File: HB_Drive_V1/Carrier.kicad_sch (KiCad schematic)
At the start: 33 parts, among them U10 NE555D, U11 TL082, U22 NE555D

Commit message: finishes hirearchical labels, add 10v +- ref generation and updates the DC offset circuits
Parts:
- removed R35, R42: PV36W104C01B00, PV36W104C01B00:POT_PV36W_BRN, symbol PV36W104C01B00:PV36W104C01B00
- removed R38, R39, R41: 51KΩ, Resistor_SMD:R_0603_1608Metric_Pad0.98x0.95mm_HandSolder, symbol Device:R_Small_US
- removed R40: 10KΩ, Resistor_SMD:R_0603_1608Metric_Pad0.98x0.95mm_HandSolder, symbol Device:R_Small_US
- removed TP8: TestPoint, TestPoint:TestPoint_Loop_D2.60mm_Drill1.6mm_Beaded, symbol Connector:TestPoint
- removed unit 2 of U11
- added C50, C51: 100pF 50V, Capacitor_SMD:C_0603_1608Metric, symbol Device:C
- added R100: PV36W104C01B00, PV36W104C01B00:POT_PV36W_BRN, symbol PV36W104C01B00:PV36W104C01B00
- added R101, R102: 10KΩ, Resistor_SMD:R_0603_1608Metric_Pad0.98x0.95mm_HandSolder, symbol Device:R_Small_US
- added R103: PV36W204C01B00, PV36W104C01B00:POT_PV36W_BRN, symbol PV36W104C01B00:PV36W104C01B00
- added TP28: TestPoint, TestPoint:TestPoint_Loop_D2.60mm_Drill1.6mm_Beaded, symbol Connector:TestPoint
- added U26: TL082, Package_SO:SOIC-8_5.3x5.3mm_P1.27mm, symbol Amplifier_Operational:TL082
- added U27: TL082, symbol Amplifier_Operational:TL082
- renumbered C18 to C41, C19 to C42, C20 to C43, C21 to C44, C22 to C45, C23 to C46, C24 to C47, C39 to C48, C42 to C49, D7 to D5, R36 to R74, R37 to R75, R43 to R81, R44 to R82, R45 to R83, R46 to R84, R71 to R85, R70 to R86, R57 to R87, TP7 to TP20, TP9 to TP22, TP10 to TP23, U10 to U19, U11 to U20, U22 to U21
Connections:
- net Bipolar Triangle Wave: now also R101.2
- net Carrier: now also R103.2, R103.3, TP28.1, U27.7
- net GND: now also U27.6 (-)
- new net: R101.1, R102.1, R103.1, U27.5 (+)
- new net: R100.2, U26.5 (+)
- new net: R102.2, U26.6 (-), U26.7
- new net +10V_Ref: R100.1
- new net -10V_Ref: R100.3
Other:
- note added: "DC Offset [0 to -10V DC]"
- note added: "TRIANGLE WAVE DC OFFSET, AND GAIN ADJUST"
- note removed: "DC Offset [0 to -15V DC]"
- note removed: "TRIANGLE WAVE DC OFFSET AND GAIN ADJUST"

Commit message: updates board to highest working copy
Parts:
- removed C46, C47: 100nF 100V, Capacitor_SMD:C_0603_1608Metric, symbol Device:C
- removed unit 3 of U20
- removed U27: TL082, symbol Amplifier_Operational:TL082
- added C1001: 100pF 50V, Capacitor_SMD:C_0603_1608Metric, symbol Device:C
- added C1009, C1011, C1013, C1014: 100nF 100V, Capacitor_SMD:C_0603_1608Metric, symbol Device:C
- added J1001: Conn_02x02_Odd_Even, Connector_PinHeader_2.54mm:PinHeader_2x02_P2.54mm_Vertical, symbol Connector_Generic:Conn_02x02_Odd_Even
- added unit 3 of U1003
- added U1004: TL082, Package_SO:SOIC-8_3.9x4.9mm_P1.27mm, symbol Amplifier_Operational:TL082
- C1002: renamed from C51; now not fitted
- C1003: renamed from C50; now not fitted
- U1002: renamed from U21; now not fitted
- U1003: renamed from U20; footprint Package_SO:SOIC-8_5.3x5.3mm_P1.27mm -> Package_SO:SOIC-8_3.9x4.9mm_P1.27mm
- U1003: renamed from U26; footprint Package_SO:SOIC-8_5.3x5.3mm_P1.27mm -> Package_SO:SOIC-8_3.9x4.9mm_P1.27mm
- renumbered C41 to C1004, C42 to C1005, C43 to C1006, C44 to C1007, C45 to C1008, C48 to C1010, C49 to C1012, D5 to D1001, D6 to D1002, R74 to R1001, R75 to R1002, R100 to R1003, R101 to R1004, R102 to R1005, R81 to R1006, R103 to R1007, R82 to R1008, R83 to R1009, R84 to R1010, R85 to R1011, R86 to R1012, R87 to R1013, TP20 to TP1001, TP22 to TP1002, TP28 to TP1003, TP23 to TP1004, U19 to U1001
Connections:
- net +15V: now also C1013.2, C1014.2, U1003.8 (V+), U1004.8 (V+)
- net -15V: now also C1009.1, C1011.1, U1003.4 (V-), U1004.4 (V-)
- net Carrier: now also U1004.7
- net GND: now also C1002.2, C1003.2, C1001.2, C1009.2, C1011.2, C1013.1, C1014.1, U1004.5 (+)
- net at C1004.1, R1002.2, U1001.2 (TRIG)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: now also C1002.1, C1003.1, C1001.1
- net at R1004.1, R1005.1, R1007.1: now also U1004.6 (-)
- net at C1010.1, D1001.2 (A), D1002.1 (K)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: no longer R1012.1
- net at D1001.1 (K): now also R1012.1
- net at TP1001.1, U1001.3 (OUT): now also J1001.3 (Pin_3); no longer C1006.2
- net Experimental Square Wave: now reaches U1002.3 (OUT)
- net Experimental Square Wave: now also J1001.1 (Pin_1)
- new net: C1006.2, J1001.2 (Pin_2), J1001.4 (Pin_4)
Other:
- moved on the sheet: D1001, D1002, R1003, R1007, R1008, R1012, TP1001, TP1002, TP1003, TP1004, U1001, U1003A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

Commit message: updates board to REV 1 Ordered version
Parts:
- added unit 1 of U1004
- R1004, R1005, R1009: value 10KΩ -> 10kΩ 1%
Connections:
- net GND: now also U1004.3 (+)
- new net: U1004.1, U1004.2 (-)
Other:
- note added: "unused OpAmp 1004A on TL082 Dual Package"
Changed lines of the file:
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@@
 	)
 	(rectangle
+		(start 87.63 95.25)
+		(end 138.43 99.06)
+		(stroke
+			(width 0)
+			(type default)
+		)
+		(fill
+			(type none)
+		)
+	)
+	(rectangle
 		(start 29.718 37.338)
 		(end 53.848 43.688)
@@
 		)
 	)
+	(text "unused OpAmp 1004A on TL082 Dual Package"
+		(exclude_from_sim no)
+		(at 113.03 97.282 0)
+		(effects
+			(font
+				(size 1.27 1.27)
+			)
+		)
+	)
 	(text "TRIANGLE WAVE DC OFFSET, AND GAIN ADJUST"
 		(exclude_from_sim no)
@@
 	(wire
 		(pts
+			(xy 76.2 110.49) (xy 91.44 110.49)
+		)
+		(stroke
+			(width 0)
+			(type default)
+		)
+	)
+	(wire
+		(pts
 			(xy 194.31 105.41) (xy 194.31 106.68)
 		)
@@
 	(wire
 		(pts
+			(xy 72.39 99.06) (xy 72.39 101.6)
+		)
+		(stroke
+			(width 0)
+			(type default)
+		)
+	)
+	(wire
+		(pts
 			(xy 105.41 110.49) (xy 105.41 118.11)
 		)
@@
 	(wire
 		(pts
+			(xy 91.44 101.6) (xy 91.44 110.49)
+		)
+		(stroke
+			(width 0)
+			(type default)
+		)
+	)
+	(wire
+		(pts
 			(xy 64.77 45.72) (xy 64.77 46.99)
 		)
@@
 	(wire
 		(pts
+			(xy 72.39 99.06) (xy 76.2 99.06)
+		)
+		(stroke
+			(width 0)
+			(type default)
+		)
+	)
+	(wire
+		(pts
 			(xy 179.07 106.68) (xy 181.61 106.68)
 		)
@@
 	(wire
 		(pts
+			(xy 76.2 104.14) (xy 76.2 110.49)
+		)
+		(stroke
+			(width 0)
+			(type default)
+		)
+	)
+	(wire
+		(pts
 			(xy 45.72 110.49) (xy 52.07 110.49)
 		)
@@
 	)
 	(symbol
+		(lib_id "Amplifier_Operational:TL082")
+		(at 83.82 101.6 0)
+		(unit 1)
+		(body_style 1)
+		(exclude_from_sim no)
+		(in_bom yes)
+		(on_board yes)
+		(in_pos_files yes)
+		(dnp no)
+		(property "Reference" "U1004"
+			(at 86.614 106.426 0)
+			(show_name no)
+			(do_not_autoplace no)
+			(effects
+				(font
+					(size 1.27 1.27)
+				)
+			)
+		)
+		(property "Value" "TL082"
+			(at 87.884 107.188 0)
+			(hide yes)
+			(show_name no)
+			(do_not_autoplace no)
+			(effects
+				(font
+					(size 1.27 1.27)
+				)
+			)
+		)
+		(property "Footprint" "Package_SO:SOIC-8_3.9x4.9mm_P1.27mm"
+			(at 83.82 101.6 0)
+			(hide yes)
+			(show_name no)
+			(do_not_autoplace no)
+			(effects
+				(font
+					(size 1.27 1.27)
+				)
+			)
+		)
+		(property "Datasheet" "http://www.ti.com/lit/ds/symlink/tl081.pdf"
+			(at 83.82 101.6 0)
+			(hide yes)
+			(show_name no)
+			(do_not_autoplace no)
+			(effects
+				(font
+					(size 1.27 1.27)
+				)
+			)
+		)
+		(property "Description" "Dual JFET-Input Operational Amplifiers, DIP-8/SOIC-8/SSOP-8"
+			(at 83.82 101.6 0)
+			(hide yes)
+			(show_name no)
+			(do_not_autoplace no)
+			(effects
+				(font
+					(size 1.27 1.27)
+				)
+			)
+		)
+		(pin "3"
+		)
+		(pin "1"
+		)
+		(pin "2"
+		)
+		(pin "6"
+		)
+		(pin "4"
+		)
+		(pin "7"
+		)
+		(pin "5"
+		)
+		(pin "8"
+		)
+		(instances
+			(project "HB_Drive_V1"
+				(path "/a9b54c89-4c8e-4c90-8a0d-ec2009e369b7/28e2d9d3-ebce-4623-8c7e-52f93025d826/14fd6338-58f3-45df-a84c-66c2fad9aa6c"
+					(reference "U1004")
+					(unit 1)
+				)
+			)
+		)
+	)
+	(symbol
 		(lib_id "power:GND")
 		(at 110.49 128.27 0)
@@
 	)
 	(symbol
+		(lib_id "power:GND")
+		(at 72.39 101.6 0)
+		(unit 1)
+		(body_style 1)
+		(exclude_from_sim no)
+		(in_bom yes)
+		(on_board yes)
+		(in_pos_files yes)
+		(dnp no)
+		(property "Reference" "#PWR01020"
+			(at 72.39 107.95 0)
+			(hide yes)
+			(show_name no)
+			(do_not_autoplace no)
+			(effects
+				(font
+					(size 1.27 1.27)
+				)
+			)
+		)
+		(property "Value" "GND"
+			(at 69.596 105.918 0)
+			(show_name no)
+			(do_not_autoplace no)
+			(effects
+				(font
+					(size 1.27 1.27)
+				)
+			)
+		)
+		(property "Footprint" ""
+			(at 72.39 101.6 0)
+			(hide yes)
+			(show_name no)
+			(do_not_autoplace no)
+			(effects
+				(font
+					(size 1.27 1.27)
+				)
+			)
+		)
+		(property "Datasheet" ""
+			(at 72.39 101.6 0)
+			(hide yes)
+			(show_name no)
+			(do_not_autoplace no)
+			(effects
+				(font
+					(size 1.27 1.27)
+				)
+			)
+		)
+		(property "Description" "Power symbol creates a global label with name \"GND\" , ground"
+			(at 72.39 101.6 0)
+			(hide yes)
+			(show_name no)
+			(do_not_autoplace no)
+			(effects
+				(font
+					(size 1.27 1.27)
+				)
+			)
+		)
+		(pin "1"
+		)
+		(instances
+			(project "HB_Drive_V1"
+				(path "/a9b54c89-4c8e-4c90-8a0d-ec2009e369b7/28e2d9d3-ebce-4623-8c7e-52f93025d826/14fd6338-58f3-45df-a84c-66c2fad9aa6c"
+					(reference "#PWR01020")
+					(unit 1)
+				)
+			)
+		)
+	)
+	(symbol
 		(lib_id "power:-15V")
 		(at 194.31 105.41 0)
@@
 			)
 		)
-		(property "Value" "10KΩ"
+		(property "Value" "10kΩ 1%"
 			(at 137.414 56.896 90)
 			(show_name no)
@@
 			)
 		)
-		(property "Value" "10KΩ"
+		(property "Value" "10kΩ 1%"
 			(at 98.806 115.062 90)
 			(show_name no)
@@
 			)
 		)
-		(property "Value" "10KΩ"
+		(property "Value" "10kΩ 1%"
 			(at 98.806 120.142 90)
 			(hide yes)

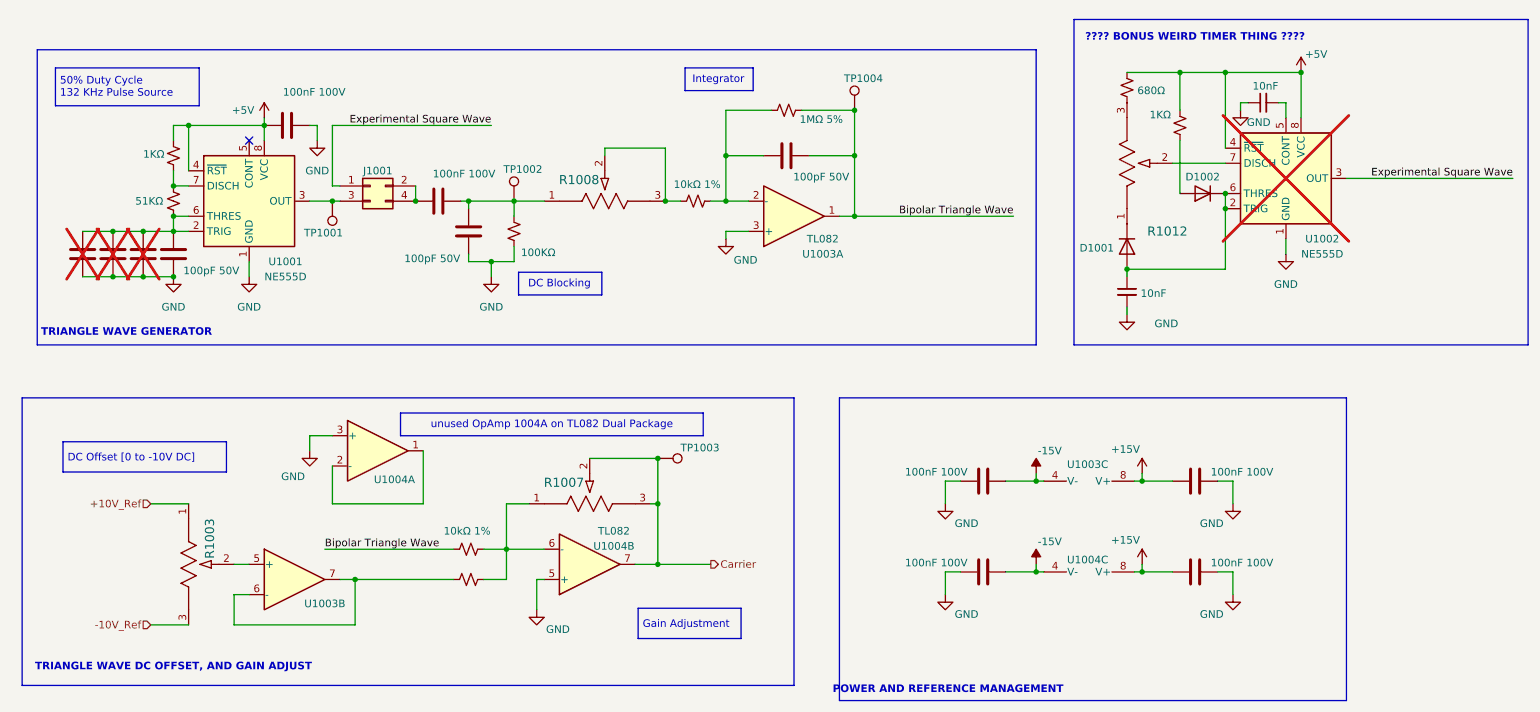
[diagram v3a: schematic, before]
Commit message: Annotates Schematic! Fixes REV1 wiring swaps and replaces buffer
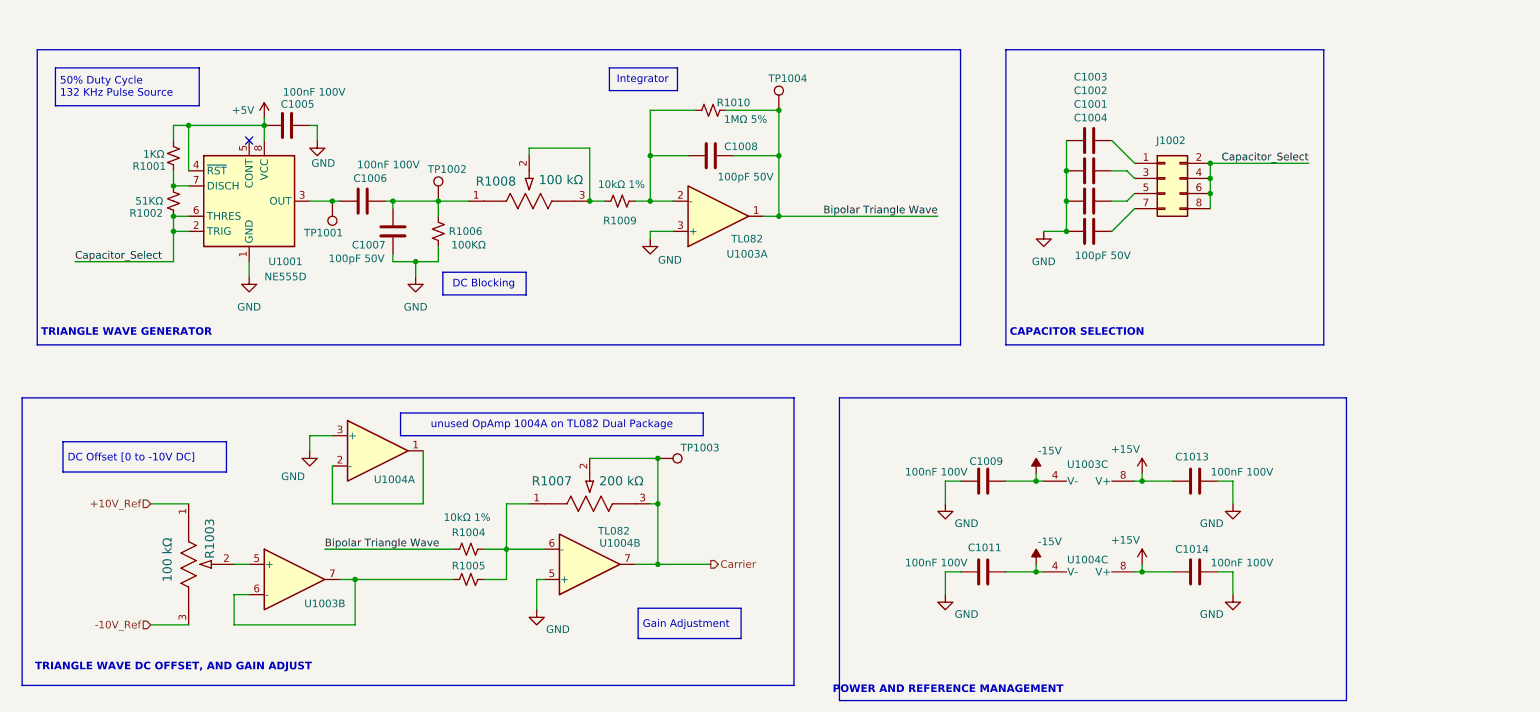
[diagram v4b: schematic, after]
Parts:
- removed C1010, C1012: 10nF, Capacitor_SMD:C_0603_1608Metric_Pad1.08x0.95mm_HandSolder, symbol Device:C_Small
- removed D1001, D1002: 1N4148W, Diode_SMD:D_SOD-123, symbol Diode:1N4148W
- removed J1001: Conn_02x02_Odd_Even, Connector_PinHeader_2.54mm:PinHeader_2x02_P2.54mm_Vertical, symbol Connector_Generic:Conn_02x02_Odd_Even
- removed R1011: 680Ω, Resistor_SMD:R_0603_1608Metric_Pad0.98x0.95mm_HandSolder, symbol Device:R_Small_US
- removed R1012: PV36W103C01B00, PV36W104C01B00:POT_PV36W_BRN, symbol PV36W103C01B00:PV36W103C01B00
- removed R1013: 1KΩ, Resistor_SMD:R_0603_1608Metric_Pad0.98x0.95mm_HandSolder, symbol Device:R_Small_US
- removed U1002: NE555D, Package_SO:SOIC-8_3.9x4.9mm_P1.27mm, symbol Timer:NE555D
- added J1002: Conn_02x04_Odd_Even, Connector_PinHeader_2.54mm:PinHeader_2x04_P2.54mm_Vertical, symbol Connector_Generic:Conn_02x04_Odd_Even
- C1001, C1002, C1003: now fitted
- R1003, R1008: value PV36W104C01B00 -> 100 kΩ
- R1007: value PV36W204C01B00 -> 200 kΩ
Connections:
- net at C1006.2: now also TP1001.1, U1001.3 (OUT)
- new net: C1003.1, J1002.1 (Pin_1)
- new net: C1002.1, J1002.3 (Pin_3)
- new net: C1001.1, J1002.5 (Pin_5)
- new net: C1004.1, J1002.7 (Pin_7)
- new net Capacitor_Select: J1002.2 (Pin_2), J1002.4 (Pin_4), J1002.6 (Pin_6), J1002.8 (Pin_8), R1002.2, U1001.2 (TRIG), U1001.6 (THRES)
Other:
- note added: "CAPACITOR SELECTION"
- note removed: "???? BONUS WEIRD TIMER THING ????"
- moved on the sheet: R1008, TP1002, TP1004, U1003A
